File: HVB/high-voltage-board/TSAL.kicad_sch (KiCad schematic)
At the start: 13 parts, among them Q1 040N03LG, Q2 040N03LG, U2 LTV-817S, U3 LM555xM

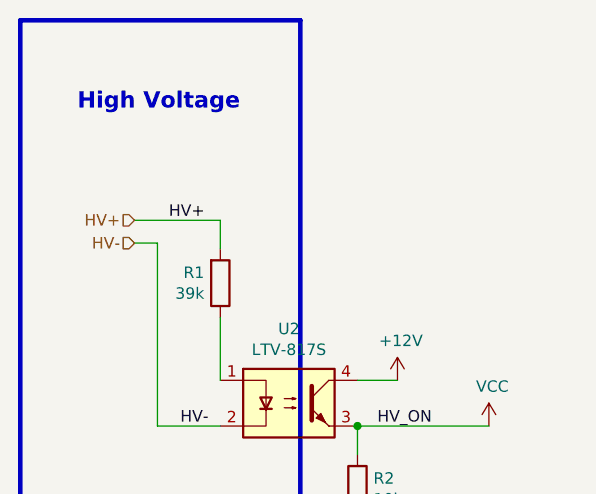
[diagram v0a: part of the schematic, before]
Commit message: working on layout
Updating traces for RCB and organizing HVB
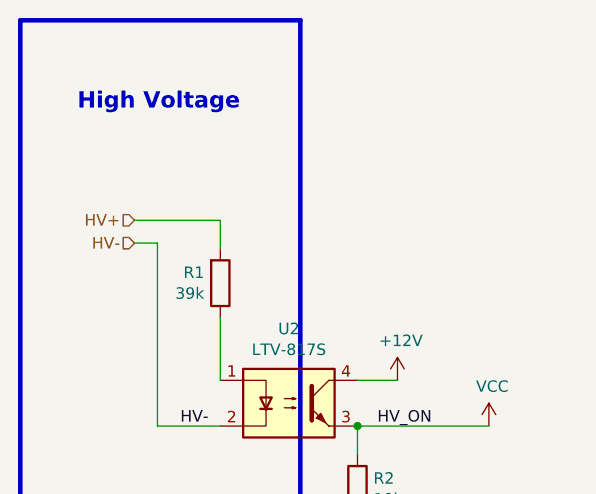
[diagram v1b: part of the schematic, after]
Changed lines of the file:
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@@
-    (effects (font (size 1.27 1.27)) (justify left bottom))
-  )
-  (label "HV+" (at 41.275 57.785 0)
     (effects (font (size 1.27 1.27)) (justify left bottom))
   )

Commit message: Layout and Footprints update
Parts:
- removed Q1, Q2: 040N03LG, Package_TO_SOT_SMD:TO-252-3_TabPin2, symbol Device:Q_NMOS_GDS
- added Q1, Q2: PSMN5R2-60YL, Package_TO_SOT_SMD:LFPAK56, symbol Transistor_FET:PSMN5R2-60YL
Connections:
- net GND: now also Q1.1 (S), Q1.2 (S), Q1.3 (S)
- net TSAL_GND: now also Q2.5 (D)
- net at R6.2: now also Q1.4 (G), Q2.1 (S), Q2.2 (S), Q2.3 (S)
- net at R5.1: now also Q1.5 (D), Q2.4 (G)
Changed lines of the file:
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@@
     (pin "1")
-  )
-  (symbol (lib_id "Device:Q_NMOS_GDS") (at 201.93 87.63 0) (mirror y) (unit 1)
-    (in_bom yes) (on_board yes)
-    (property "Reference" "Q1" (id 0) (at 196.7484 86.4616 0)
-      (effects (font (size 1.27 1.27)) (justify left))
-    )
-    (property "Value" "040N03LG" (id 1) (at 196.7484 88.773 0)
-      (effects (font (size 1.27 1.27)) (justify left))
-    )
-    (property "Footprint" "Package_TO_SOT_SMD:TO-252-3_TabPin2" (id 2) (at 196.85 85.09 0)
-      (effects (font (size 1.27 1.27)) hide)
-    )
-    (property "Datasheet" "https://media.digikey.com/pdf/Data%20Sheets/Infineon%20PDFs/IPD040N03LG_rev1.01.pdf" (id 3) (at 201.93 87.63 0)
-      (effects (font (size 1.27 1.27)) hide)
-    )
-    (pin "1")
-    (pin "2")
-    (pin "3")
   )
   (symbol (lib_id "Device:R") (at 190.5 77.47 270) (unit 1)
@@
     (pin "2")
   )
-  (symbol (lib_id "Device:Q_NMOS_GDS") (at 207.645 77.47 0) (unit 1)
-    (in_bom yes) (on_board yes)
-    (property "Reference" "Q2" (id 0) (at 212.8266 76.3016 0)
-      (effects (font (size 1.27 1.27)) (justify left))
-    )
-    (property "Value" "040N03LG" (id 1) (at 212.8266 78.613 0)
-      (effects (font (size 1.27 1.27)) (justify left))
-    )
-    (property "Footprint" "Package_TO_SOT_SMD:TO-252-3_TabPin2" (id 2) (at 212.725 74.93 0)
-      (effects (font (size 1.27 1.27)) hide)
-    )
-    (property "Datasheet" "https://media.digikey.com/pdf/Data%20Sheets/Infineon%20PDFs/IPD040N03LG_rev1.01.pdf" (id 3) (at 207.645 77.47 0)
-      (effects (font (size 1.27 1.27)) hide)
-    )
-    (pin "1")
-    (pin "2")
-    (pin "3")
-  )
   (symbol (lib_id "Device:C") (at 119.38 60.325 0) (unit 1)
     (in_bom yes) (on_board yes)
@@
     (pin "1")
   )
+  (symbol (lib_id "Transistor_FET:PSMN5R2-60YL") (at 201.93 87.63 0) (mirror y) (unit 1)
+    (in_bom yes) (on_board yes) (fields_autoplaced)
+    (property "Reference" "Q1" (id 0) (at 196.723 86.7215 0)
+      (effects (font (size 1.27 1.27)) (justify left))
+    )
+    (property "Value" "PSMN5R2-60YL" (id 1) (at 196.723 89.4966 0)
+      (effects (font (size 1.27 1.27)) (justify left))
+    )
+    (property "Footprint" "Package_TO_SOT_SMD:LFPAK56" (id 2) (at 198.12 87.63 0)
+      (effects (font (size 1.27 1.27)) hide)
+    )
+    (property "Datasheet" "https://assets.nexperia.com/documents/data-sheet/PSMN5R2-60YL.pdf" (id 3) (at 201.93 87.63 0)
+      (effects (font (size 1.27 1.27)) hide)
+    )
+    (pin "1")
+    (pin "2")
+    (pin "3")
+    (pin "4")
+    (pin "5")
+  )
+  (symbol (lib_id "Transistor_FET:PSMN5R2-60YL") (at 207.645 77.47 0) (unit 1)
+    (in_bom yes) (on_board yes) (fields_autoplaced)
+    (property "Reference" "Q2" (id 0) (at 212.852 76.5615 0)
+      (effects (font (size 1.27 1.27)) (justify left))
+    )
+    (property "Value" "PSMN5R2-60YL" (id 1) (at 212.852 79.3366 0)
+      (effects (font (size 1.27 1.27)) (justify left))
+    )
+    (property "Footprint" "Package_TO_SOT_SMD:LFPAK56" (id 2) (at 211.455 77.47 0)
+      (effects (font (size 1.27 1.27)) hide)
+    )
+    (property "Datasheet" "https://assets.nexperia.com/documents/data-sheet/PSMN5R2-60YL.pdf" (id 3) (at 207.645 77.47 0)
+      (effects (font (size 1.27 1.27)) hide)
+    )
+    (pin "1")
+    (pin "2")
+    (pin "3")
+    (pin "4")
+    (pin "5")
+  )
 )

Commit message: Addded comments
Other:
- note added: "Check footprint/ device mounting, add actual part number"
- note added: "DC/DC Power"
- note added: "not sure why but this doesnt work with a 51k for R3 and a 683k + 237k in series for R4 now its about 3Hz cycle CONFUSED"
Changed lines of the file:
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@@
     (stroke (width 0) (type default) (color 0 0 0 0))
+  )
+  (text "Check footprint/ device mounting, add actual part number"
+    (at 106.045 47.625 0)
+    (effects (font (size 1.27 1.27) bold italic) (justify left bottom))
+  )
+  (text "DC/DC Power" (at 62.23 69.85 0)
+    (effects (font (size 1.27 1.27) bold italic) (justify left bottom))
   )
   (text "Change R6 for \nCurrent Rating" (at 216.535 93.345 0)
@@
     (effects (font (size 1.8034 1.8034) (thickness 0.3607) bold) (justify left bottom))
   )
+  (text "not sure why \nbut this doesnt work \nwith a 51k for R3 and a 683k + 237k in series for R4\nnow its about 3Hz cycle\nCONFUSED"
+    (at 179.07 125.73 0)
+    (effects (font (size 1.27 1.27) bold italic) (justify left bottom))
+  )
   (label "HV_ON" (at 132.715 67.945 90)
